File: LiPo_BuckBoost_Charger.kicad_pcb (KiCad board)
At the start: 4 copper layers, 53 x 33 mm, 56 parts, among them J1 Type-C_6P, J2 JST PH Connector, J3 Conn_01x01, J4 Conn_01x01, J5 JST PH Connector, J6 JST PH Connector, J7 JST PH Connector, U1 TP4056, U2 DW01A, U3 FS8205A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

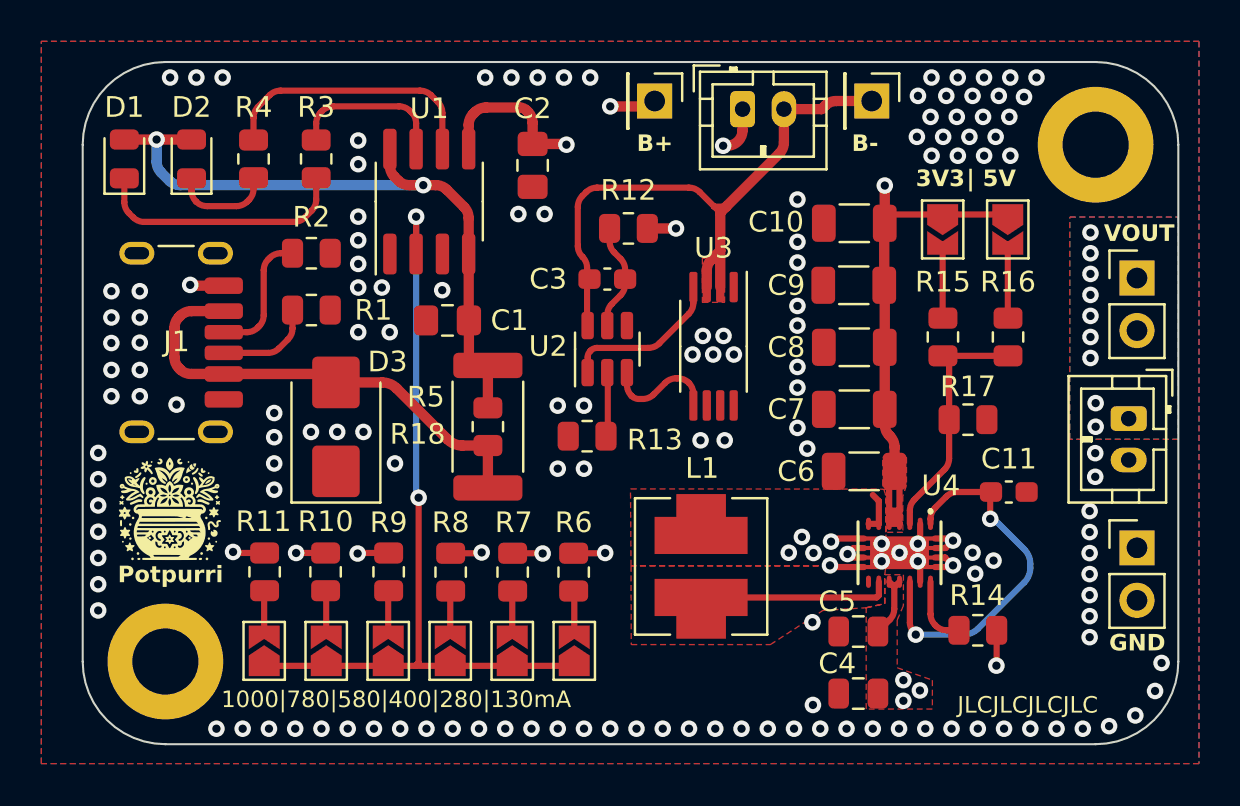
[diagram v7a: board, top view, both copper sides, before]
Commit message: version 1.3 - added circuit which disconnects battery from load during charging
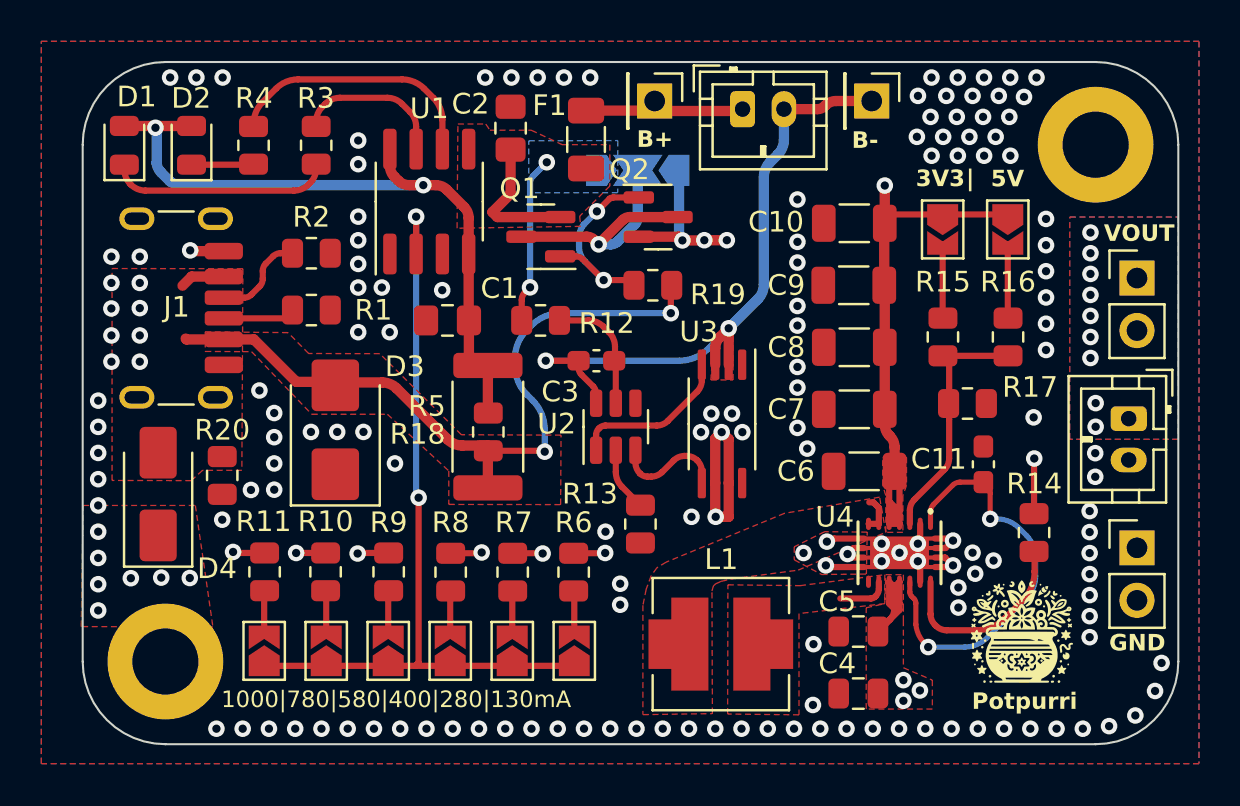
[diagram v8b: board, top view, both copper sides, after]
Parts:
- added D4: SS34, Diode_SMD:D_SMA, F.Cu at (74.7, 43.9)
- added F1: 1.5A, Fuse:Fuse_1206_3216Metric, F.Cu at (95.3, 26.8)
- added JP9: SolderJumper_3_Open, Jumper:SolderJumper-3_P2.0mm_Open_TrianglePad1.0x1.5mm, B.Cu at (97.8, 28.2)
- added Q1: SI2301, Package_TO_SOT_SMD:SOT-23, F.Cu at (93.2, 31.4)
- added Q2: SI2301, Package_TO_SOT_SMD:SOT-23, F.Cu at (98.8, 30.5)
- added R19: R, Resistor_SMD:R_0805_2012Metric, F.Cu at (98.6, 33.8)
- added R20: 10k, Resistor_SMD:R_0805_2012Metric, F.Cu at (77.8, 43.0)
- R5: value 0R2 to 0R5 -> 0R4
- moved G*** 41.6 mm to (116.5, 50.6)
- moved R12 6.15 mm to (93.2, 35.5), turned to 180 degrees
- moved R14 5.46 mm to (117.0, 45.8), turned to -90 degrees
- moved R13 4.97 mm to (98.0, 45.4), turned to -90 degrees
- moved C3 3.99 mm to (95.8, 37.5)
- moved L1 3.82 mm to (101.9, 51.1), turned to -90 degrees
- moved U3 3.78 mm to (101.9, 40.5)
- moved U2 3.78 mm to (96.8, 40.6)
- moved C2 2.09 mm to (91.7, 26.2), turned to 90 degrees
- moved C11 1.82 mm to (114.6, 42.5), turned to 90 degrees
- moved J1 1.67 mm to (70.5, 34.9)
- moved R17 0.78 mm to (113.8, 39.5)
- moved D1 0.66 mm to (73.0, 27.0)
- moved D2 0.66 mm to (76.3, 27.0)
- moved R3 0.66 mm to (82.3, 27.0)
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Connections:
- C2 pad 1: +BATT -> Net-(JP9-A)
- C4 pad 1: +BATT -> VCC
- C5 pad 1: +BATT -> VCC
- R12 pad 2: +BATT -> Net-(JP9-A)
- U1 pad 5: +BATT -> Net-(JP9-A)
- U4 pad 10: +BATT -> VCC
- U4 pad 11: +BATT -> VCC
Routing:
- net VBUS: track 23.2 -> 39.8 mm, vias 0 -> 2
- net VCC: track 0.00 -> 15.6 mm, vias 0 -> 9
- net Net-(JP9-A): track 0.00 -> 14.9 mm, vias 0 -> 2
- net Net-(JP9-C): track 0.00 -> 13.0 mm, vias 0 -> 1
- net Net-(Q1-G): track 0.00 -> 10.4 mm, vias 0 -> 2
- net GND: track 25.8 -> 34.9 mm, vias 160 -> 168
- net +BATT: track 17.0 -> 8.72 mm, vias 7 -> 0
- net Net-(L1-Pad1): track 9.30 -> 2.48 mm
- net Net-(U4-PG): track 3.37 -> 9.49 mm
- net -BATT: track 30.6 -> 33.0 mm, vias 0 -> 2
- net +5V: track 29.2 -> 31.2 mm
- net Net-(U4-EN): track 18.0 -> 20.1 mm
- net Net-(D2-K): track 5.01 -> 3.01 mm
- net Net-(J1-CC1): track 6.40 -> 4.59 mm
- net Net-(D1-K): track 12.6 -> 10.9 mm
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- added copper zone on B.Cu, net Net-(JP9-A)
- added copper zone on F.Cu, net Net-(JP9-A)
- added copper zone on F.Cu, net VBUS
- added copper zone on F.Cu, net VCC
- added copper zone on In2.Cu, net VCC
- removed copper zone on F.Cu, net +BATT
- removed copper zone on In2.Cu, net +BATT
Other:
- board text added: "5V"
- board text added: "Load cut-off bypass"
- board text added: "Q1"
- board text added: "Q2"
- board text added: "|"
- board text removed: "| 5V"
